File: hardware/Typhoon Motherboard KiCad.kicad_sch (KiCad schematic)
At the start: 14 parts, among them J1 Conn_01x04_Pin, J2 Conn_02x03_Odd_Even, P1 USB_C_Plug_USB2.0, U1 ESP32-S3-WROOM-1, U2 AZ1117-3.3

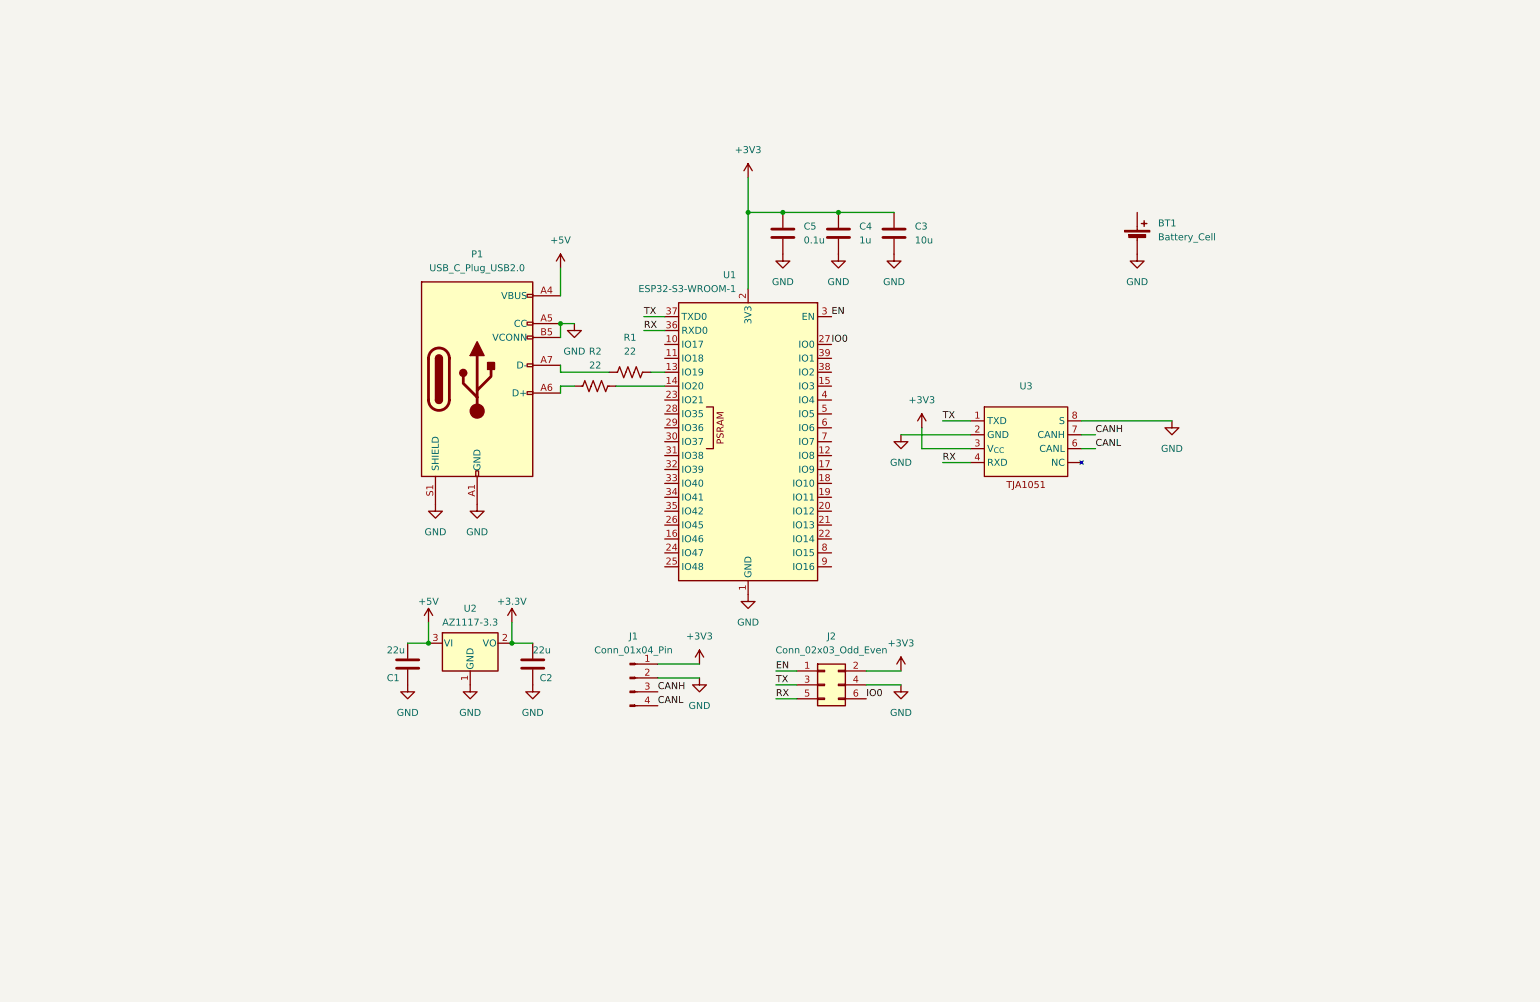
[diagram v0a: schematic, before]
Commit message: first version of motherboard schematic
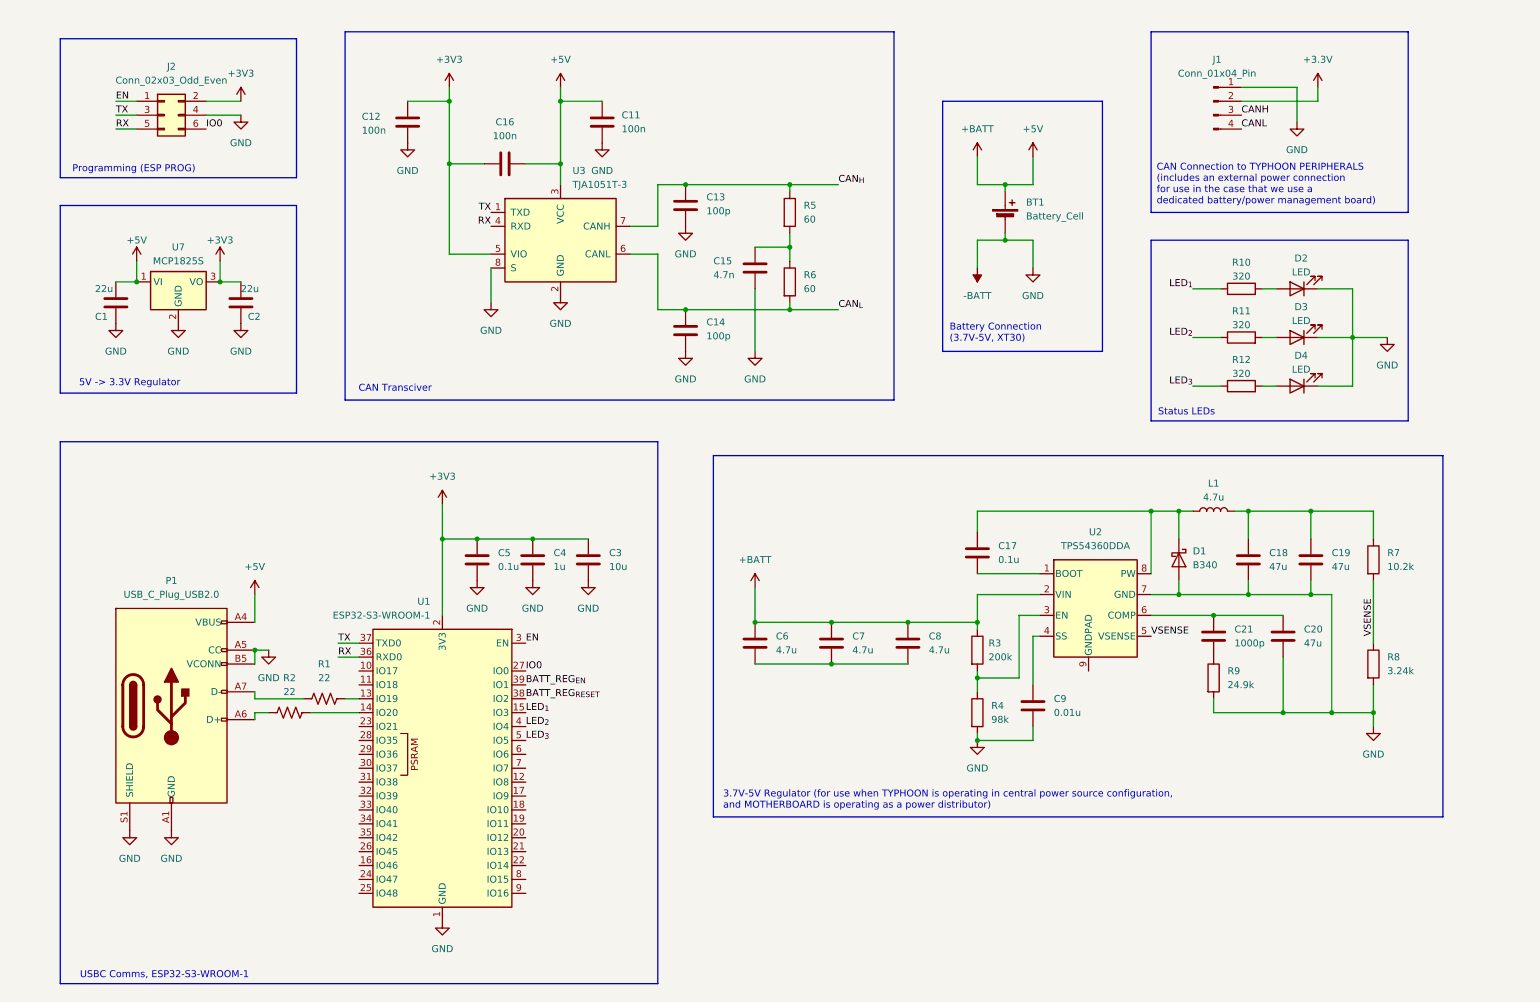
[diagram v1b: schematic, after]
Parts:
- removed U2: AZ1117-3.3, Package_TO_SOT_SMD:SOT-223-3_TabPin2, symbol Regulator_Linear:AZ1117-3.3
- removed U3: ~, Package_SO:SO-8_3.9x4.9mm_P1.27mm, symbol Interface_CAN_LIN:TJA1051
- added C11, C12, C16: 100n, symbol Device:C
- added C13, C14: 100p, symbol Device:C
- added C15: 4.7n, symbol Device:C
- added C17: 0.1u, symbol Device:C
- added C18, C19, C20: 47u, symbol Device:C
- added C21: 1000p, symbol Device:C
- added C6, C7, C8: 4.7u, symbol Device:C
- added C9: 0.01u, symbol Device:C
- added D1: B340, Diode_SMD:D_SMC, symbol Diode:B340
- added D2, D3, D4: LED, symbol Device:LED
- added L1: 4.7u, symbol Device:L
- added R10, R11, R12: 320, symbol Device:R
- added R3: 200k, symbol Device:R
- added R4: 98k, symbol Device:R
- added R5, R6: 60, symbol Device:R
- added R7: 10.2k, symbol Device:R
- added R8: 3.24k, symbol Device:R
- added R9: 24.9k, symbol Device:R
- added U2: TPS54360DDA, Package_SO:TI_SO-PowerPAD-8_ThermalVias, symbol Regulator_Switching:TPS54360DDA
- added U3: TJA1051T-3, Package_SO:SOIC-8_3.9x4.9mm_P1.27mm, symbol Interface_CAN_LIN:TJA1051T-3
- added U7: MCP1825S, Package_TO_SOT_SMD:SOT-223-3_TabPin2, symbol Regulator_Linear:MCP1825S
- BT1: footprint Connector_AMASS:AMASS_XT30U-M_1x02_P5.0mm_Vertical -> Connector_AMASS:AMASS_XT30PW-M_1x02_P2.50mm_Horizontal
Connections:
- net +3.3V: now also J1.2 (Pin_2); no longer C2.2
- net +3V3: now also C2.2, C12.1, C16.1, U3.5 (VIO), U7.3 (VO); no longer J1.1 (Pin_1)
- net +5V: now also BT1.1 (+), C11.1, C16.2, C6.1, C7.1, C8.1, R3.1, U2.2 (VIN), U3.3 (VCC), U7.1 (VI)
- net RX: now also U3.4 (RXD)
- net TX: now also U3.1 (TXD)
- net LED_{1}: now reaches U1.15 (IO3)
- net LED_{1}: now also R10.1
- net BATT_REG_{RESET}: now reaches U1.38 (IO2)
- net BATT_REG_{EN}: now reaches U1.39 (IO1)
- net LED_{2}: now reaches U1.4 (IO4)
- net LED_{2}: now also R11.1
- net LED_{3}: now reaches U1.5 (IO5)
- net LED_{3}: now also R12.1
- net GND renamed -BATT
- net -BATT: now also J1.1 (Pin_1), C11.2, C12.2, C13.2, C14.2, C15.2, C18.2, C19.2, C20.2, C9.2, D1.2 (A), D2.1 (K), D3.1 (K), D4.1 (K), R4.2, R8.2, R9.2, U2.7 (GND), U3.2 (GND), U3.8 (S), U7.2 (GND); no longer J1.2 (Pin_2)
- new net: D2.2 (A), R10.2
- new net: C15.1, R5.2, R6.1
- new net: R3.2, R4.1, U2.3 (EN)
- new net: C17.2, U2.1 (BOOT)
- new net: C9.1, U2.4 (SS)
- new net: C20.1, C21.1, U2.6 (COMP)
- new net: C17.1, D1.1 (K), L1.1, U2.8 (PW)
- new net: D4.2 (A), R12.2
- new net: D3.2 (A), R11.2
- new net: C6.2, C7.2, C8.2
- new net: C18.1, C19.1, L1.2, R7.1
- new net: C21.2, R9.1
- new net CAN_{H}: C13.1, R5.1, U3.7 (CANH)
- new net CAN_{L}: C14.1, R6.2, U3.6 (CANL)
- new net VSENSE: R7.2, R8.1, U2.5 (VSENSE)
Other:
- note added: "3.7V-5V Regulator (for use when TYPHOON is operating in central power source configuration, and MOTHERBOARD is operating as a power distributor)"
- note added: "5V -> 3.3V Regulator"
- note added: "Battery Connection (3.7V-5V, XT30)"
- note added: "CAN Connection to TYPHOON PERIPHERALS (includes an external power connection for use in the case that we use a dedicated battery/power management board)"
- note added: "CAN Transciver"
- note added: "Programming (ESP PROG)"
- note added: "Status LEDs"
- note added: "USBC Comms, ESP32-S3-WROOM-1"
- moved on the sheet: C1, C2, C3, C4, C5, J1, J2, P1, R1, R2, U1

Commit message: added notes
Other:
- note added: "still to do: - add uart conenction for telemetry - add power out connections for peripheral boards when in wired power operation mode"
- moved on the sheet: BT1
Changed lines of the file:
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@@
 	)
 	(junction
-		(at 194.31 45.72)
+		(at 194.31 33.02)
 		(diameter 0)
 		(color 0 0 0 0)
 	)
 	(junction
-		(at 194.31 55.88)
+		(at 194.31 43.18)
 		(diameter 0)
 		(color 0 0 0 0)
@@
 	(wire
 		(pts
-			(xy 189.23 60.96) (xy 189.23 55.88)
+			(xy 189.23 48.26) (xy 189.23 43.18)
 		)
 		(stroke
@@
 	(wire
 		(pts
-			(xy 199.39 60.96) (xy 199.39 55.88)
+			(xy 199.39 48.26) (xy 199.39 43.18)
 		)
 		(stroke
@@
 	(wire
 		(pts
-			(xy 194.31 55.88) (xy 194.31 54.61)
+			(xy 194.31 43.18) (xy 194.31 41.91)
 		)
 		(stroke
@@
 	(wire
 		(pts
-			(xy 199.39 55.88) (xy 194.31 55.88)
+			(xy 199.39 43.18) (xy 194.31 43.18)
 		)
 		(stroke
@@
 	(wire
 		(pts
-			(xy 189.23 45.72) (xy 194.31 45.72)
+			(xy 189.23 33.02) (xy 194.31 33.02)
 		)
 		(stroke
@@
 	(wire
 		(pts
-			(xy 199.39 40.64) (xy 199.39 45.72)
+			(xy 199.39 27.94) (xy 199.39 33.02)
 		)
 		(stroke
@@
 	(wire
 		(pts
-			(xy 189.23 40.64) (xy 189.23 45.72)
+			(xy 189.23 27.94) (xy 189.23 33.02)
 		)
 		(stroke
@@
 	(wire
 		(pts
-			(xy 194.31 45.72) (xy 194.31 46.99)
+			(xy 194.31 33.02) (xy 194.31 34.29)
 		)
 		(stroke
@@
 	(wire
 		(pts
-			(xy 199.39 45.72) (xy 194.31 45.72)
+			(xy 199.39 33.02) (xy 194.31 33.02)
 		)
 		(stroke
@@
 	(wire
 		(pts
-			(xy 189.23 55.88) (xy 194.31 55.88)
+			(xy 189.23 43.18) (xy 194.31 43.18)
 		)
 		(stroke
@@
 	)
 	(rectangle
-		(start 182.88 30.48)
-		(end 212.09 76.2)
+		(start 182.88 17.78)
+		(end 212.09 63.5)
 		(stroke
 			(width 0)
@@
 		)
 	)
+	(text "still to do:\n\n- add uart conenction\nfor telemetry\n\n- add power out connections\nfor peripheral boards when\nin wired power operation mode"
+		(exclude_from_sim no)
+		(at 183.134 76.962 0)
+		(effects
+			(font
+				(size 1.27 1.27)
+			)
+			(justify left)
+		)
+	)
 	(text "Battery Connection\n(3.7V-5V, XT30)"
 		(exclude_from_sim no)
-		(at 184.15 72.898 0)
+		(at 184.15 60.198 0)
 		(effects
 			(font
@@
 	(symbol
 		(lib_id "power:+BATT")
-		(at 189.23 40.64 0)
+		(at 189.23 27.94 0)
 		(unit 1)
 		(exclude_from_sim no)
@@
 		(dnp no)
 		(property "Reference" "#PWR015"
-			(at 189.23 44.45 0)
+			(at 189.23 31.75 0)
 			(effects
 				(font
@@
 		)
 		(property "Value" "+BATT"
-			(at 189.23 35.56 0)
+			(at 189.23 22.86 0)
 			(effects
 				(font
@@
 		)
 		(property "Footprint" ""
-			(at 189.23 40.64 0)
+			(at 189.23 27.94 0)
 			(effects
 				(font
@@
 		)
 		(property "Datasheet" ""
-			(at 189.23 40.64 0)
+			(at 189.23 27.94 0)
 			(effects
 				(font
@@
 		)
 		(property "Description" "Power symbol creates a global label with name \"+BATT\""
-			(at 189.23 40.64 0)
+			(at 189.23 27.94 0)
 			(effects
 				(font
@@
 	(symbol
 		(lib_id "power:GND")
-		(at 199.39 60.96 0)
+		(at 199.39 48.26 0)
 		(unit 1)
 		(exclude_from_sim no)
@@
 		(fields_autoplaced yes)
 		(property "Reference" "#PWR027"
-			(at 199.39 67.31 0)
+			(at 199.39 54.61 0)
 			(effects
 				(font
@@
 		)
 		(property "Value" "GND"
-			(at 199.39 66.04 0)
+			(at 199.39 53.34 0)
 			(effects
 				(font
@@
 		)
 		(property "Footprint" ""
-			(at 199.39 60.96 0)
+			(at 199.39 48.26 0)
 			(effects
 				(font
@@
 		)
 		(property "Datasheet" ""
-			(at 199.39 60.96 0)
+			(at 199.39 48.26 0)
 			(effects
 				(font
@@
 		)
 		(property "Description" "Power symbol creates a global label with name \"GND\" , ground"
-			(at 199.39 60.96 0)
+			(at 199.39 48.26 0)
 			(effects
 				(font
@@
 	(symbol
 		(lib_id "power:-BATT")
-		(at 189.23 60.96 180)
+		(at 189.23 48.26 180)
 		(unit 1)
 		(exclude_from_sim no)
@@
 		(fields_autoplaced yes)
 		(property "Reference" "#PWR025"
-			(at 189.23 57.15 0)
+			(at 189.23 44.45 0)
 			(effects
 				(font
@@
 		)
 		(property "Value" "-BATT"
-			(at 189.23 66.04 0)
+			(at 189.23 53.34 0)
 			(effects
 				(font
@@
 		)
 		(property "Footprint" ""
-			(at 189.23 60.96 0)
+			(at 189.23 48.26 0)
 			(effects
 				(font
@@
 		)
 		(property "Datasheet" ""
-			(at 189.23 60.96 0)
+			(at 189.23 48.26 0)
 			(effects
 				(font
@@
 		)
 		(property "Description" "Power symbol creates a global label with name \"-BATT\""
-			(at 189.23 60.96 0)
+			(at 189.23 48.26 0)
 			(effects
 				(font
@@
 	(symbol
 		(lib_id "power:+5V")
-		(at 199.39 40.64 0)
+		(at 199.39 27.94 0)
 		(unit 1)
 		(exclude_from_sim no)
@@
 		(fields_autoplaced yes)
 		(property "Reference" "#PWR042"
-			(at 199.39 44.45 0)
+			(at 199.39 31.75 0)
 			(effects
 				(font
@@
 		)
 		(property "Value" "+5V"
-			(at 199.39 35.56 0)
+			(at 199.39 22.86 0)
 			(effects
 				(font
@@
 		)
 		(property "Footprint" ""
-			(at 199.39 40.64 0)
+			(at 199.39 27.94 0)
 			(effects
 				(font
@@
 		)
 		(property "Datasheet" ""
-			(at 199.39 40.64 0)
+			(at 199.39 27.94 0)
 			(effects
 				(font
@@
 		)
 		(property "Description" "Power symbol creates a global label with name \"+5V\""
-			(at 199.39 40.64 0)
+			(at 199.39 27.94 0)
 			(effects
 				(font
@@
 	(symbol
 		(lib_id "Device:Battery_Cell")
-		(at 194.31 52.07 0)
+		(at 194.31 39.37 0)
 		(unit 1)
 		(exclude_from_sim no)
@@
 		(fields_autoplaced yes)
 		(property "Reference" "BT1"
-			(at 198.12 48.9584 0)
+			(at 198.12 36.2584 0)
 			(effects
 				(font
@@
 		)
 		(property "Value" "Battery_Cell"
-			(at 198.12 51.4984 0)
+			(at 198.12 38.7984 0)
 			(effects
 				(font
@@
 		)
 		(property "Footprint" "Connector_AMASS:AMASS_XT30PW-M_1x02_P2.50mm_Horizontal"
-			(at 194.31 50.546 90)
+			(at 194.31 37.846 90)
 			(effects
 				(font
@@
 		)
 		(property "Datasheet" "~"
-			(at 194.31 50.546 90)
+			(at 194.31 37.846 90)
 			(effects
 				(font
@@
 		)
 		(property "Description" "Single-cell battery"
-			(at 194.31 52.07 0)
+			(at 194.31 39.37 0)
 			(effects
 				(font

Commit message: Rev 2 upload
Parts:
- added J3: Conn_01x04_Pin, Connector_PinHeader_1.27mm:PinHeader_1x04_P1.27mm_Vertical, symbol Connector:Conn_01x04_Pin
- added J4, J5, J6, J7, J8, J9: Conn_01x02_Pin, Connector_PinHeader_2.00mm:PinHeader_1x02_P2.00mm_Vertical_SMD_Pin1Right, symbol Connector:Conn_01x02_Pin
- C11, C12, C13, C14, C15, C16, C17, C18, C19, C20, C21, C3, C4, C5, C6, C7, C8, C9: footprint (none) -> Capacitor_SMD:C_0603_1608Metric
- D2, D3, D4: footprint (none) -> LED_SMD:LED_0805_2012Metric
- L1: footprint (none) -> Inductor_SMD:L_Taiyo-Yuden_NR-60xx
- R1, R10, R11, R12, R2, R3, R4, R5, R6, R7, R8: footprint (none) -> Resistor_SMD:R_0603_1608Metric
- R9: value 24.9k -> 29.4k; footprint (none) -> Resistor_SMD:R_0603_1608Metric
- U2: value TPS54360DDA -> TPS54331DDA
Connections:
- net CANH is gone; now on net CAN_{H}: J1.3 (Pin_3)
- net CANL is gone; now on net CAN_{L}: J1.4 (Pin_4)
- net +3.3V: now also J3.2 (Pin_2)
- net -BATT: now also J3.1 (Pin_1), J4.2 (Pin_2), J5.2 (Pin_2), J6.2 (Pin_2), J7.2 (Pin_2), J8.2 (Pin_2), J9.2 (Pin_2)
- net D-: now reaches R1.2, U1.13 (IO19)
- net D+: now reaches R2.2, U1.14 (IO20)
- net Mother_{TX}: now reaches U1.10 (IO17)
- net Mother_{TX}: now also J3.3 (Pin_3)
- net Mother_{RX}: now reaches U1.11 (IO18)
- net Mother_{RX}: now also J3.4 (Pin_4)
- net V_{out}: now reaches C18.1, C19.1, L1.2, R7.1
- net V_{out}: now also J4.1 (Pin_1), J5.1 (Pin_1), J6.1 (Pin_1), J7.1 (Pin_1), J8.1 (Pin_1), J9.1 (Pin_1)
- net BATT_REG_{EN}: no longer names the net of U1.39 (IO1)
- net BATT_REG_{RESET}: no longer names the net of U1.38 (IO2)
- net RX renamed Prog/TypeC_{RX}
- net TX renamed Prog/TypeC_{TX}
- no-connect marks 0 -> 27
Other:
- note added: "Connection pins for peripherals for central power src config"
- note added: "ESP32-S3-WROOM-1"
- note added: "Header for connection to telemetry; UART cross over happening here"
- note added: "UART Usage warning: Due to # of UART sets, Prog and Type C UART connections will use the same set on ESP32; WHEN TYPE C is connected, Debugger should NOT be connected with anything, and vice versa"
- note added: "USB type C"
- note removed: "USBC Comms, ESP32-S3-WROOM-1"
- note removed: "still to do: - add uart conenction for telemetry - add power out connections for peripheral boards when in wired power operation mode"
- moved on the sheet: BT1, C1, C11, C12, C13, C14, C15, C16, C17, C18, C19, C2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

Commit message: revision 1 by savo
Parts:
- removed C16: 100n, Capacitor_SMD:C_0603_1608Metric, symbol Device:C
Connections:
- net -BATT is gone; now on net GND: BT1.2 (-), C1.1, C11.2, C12.2, C13.2, C14.2, C15.2, C18.2, C19.2, C2.1, C20.2, C3.2, C4.2, C5.2, C9.2, D1.2 (A), D2.1 (K), D3.1 (K), D4.1 (K), J1.1 (Pin_1), J2.4 (Pin_4), J3.1 (Pin_1), J4.2 (Pin_2), J5.2 (Pin_2), J6.2 (Pin_2), J7.2 (Pin_2), J8.2 (Pin_2), J9.2 (Pin_2), P1.A1 (GND), P1.A12 (GND), P1.A5 (CC), P1.B1 (GND), P1.B12 (GND), P1.B5 (VCONN), P1.S1 (SHIELD), R4.2, R8.2, R9.2, U1.1 (GND), U1.40 (GND), U1.41 (GND), U2.7 (GND), U3.2 (GND), U3.8 (S), U7.2 (GND)
- net +5V: no longer BT1.1 (+), C6.1, C7.1, C8.1, R3.1, U2.2 (VIN)
- net GND: now reaches C6.2, C7.2, C8.2
- net V_{out} renamed +3.3VA
- new net +BATT: BT1.1 (+), C6.1, C7.1, C8.1, R3.1, U2.2 (VIN)
